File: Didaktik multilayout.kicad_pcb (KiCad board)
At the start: 2 copper layers, 212.7 x 79.4 mm, 121 parts, among them J1 Conn_01x04_MountingPin, J2 AVR-ISP-6, SW1 SW_Push_45deg, SW10 SW_Push_45deg, SW11 SW_Push_45deg, SW12 SW_Push_45deg, SW13 SW_Push_45deg, SW14 SW_Push_45deg, SW15 SW_Push_45deg, SW16 SW_Push_45deg, SW17 SW_Push_45deg, SW18 SW_Push_45deg, SW19 SW_Push_45deg, SW2 SW_Push_45deg, SW20 SW_Push_45deg, SW21 SW_Push_45deg, SW22 SW_Push_45deg, SW23 SW_Push_45deg, SW24 SW_Push_45deg, SW25 SW_Push_45deg, SW26 SW_Push_45deg, SW27 SW_Push_45deg, SW28 SW_Push_45deg, SW29 SW_Push_45deg, SW3 SW_Push_45deg, SW30 SW_Push_45deg, SW31 SW_Push_45deg, SW31a1 SW_Push_45deg, SW32 SW_Push_45deg, SW32a1 SW_Push_45deg, SW33 SW_Push_45deg, SW33a1 SW_Push_45deg, SW34 SW_Push_45deg, SW34a1 SW_Push_45deg, SW34b1 SW_Push_45deg, SW35 SW_Push_45deg, SW35a1 SW_Push_45deg, SW35b1 SW_Push_45deg, SW35c1 SW_Push_45deg, SW36 SW_Push_45deg, SW36a1 SW_Push_45deg, SW36b1 SW_Push_45deg, SW36c1 SW_Push_45deg, SW37 SW_Push_45deg, SW37a1 SW_Push_45deg, SW37b1 SW_Push_45deg, SW38 SW_Push_45deg, SW38a1 SW_Push_45deg, SW39 SW_Push_45deg, SW39a1 SW_Push_45deg, SW4 SW_Push_45deg, SW40 SW_Push_45deg, SW40a1 SW_Push_45deg, SW5 SW_Push_45deg, SW6 SW_Push_45deg, SW7 SW_Push_45deg, SW8 SW_Push_45deg, SW9 SW_Push_45deg, U1 ATmega32U4-M, Y1 Crystal_GND24_Small

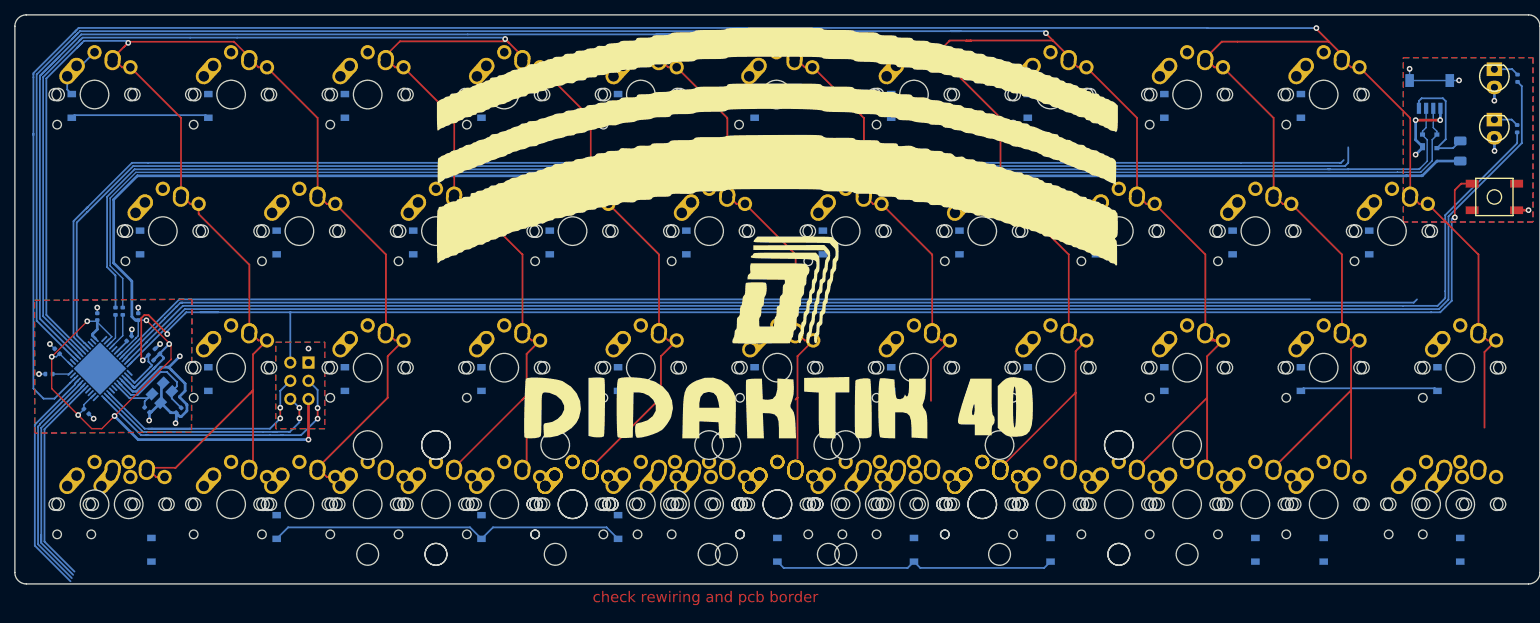
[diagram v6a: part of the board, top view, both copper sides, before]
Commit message: routing new simpler matrix on pcb
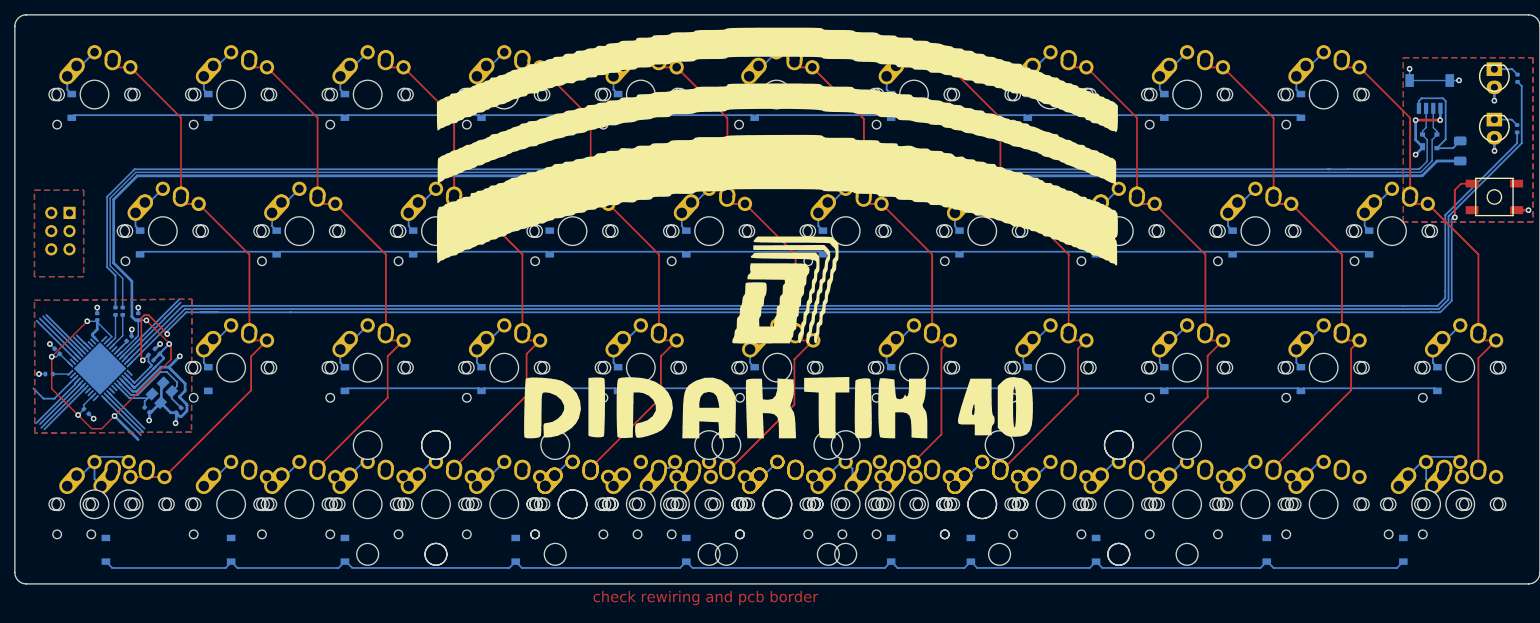
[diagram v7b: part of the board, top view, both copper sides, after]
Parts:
- moved J2 39.3 mm to (36.5, 60.3)
- moved D33 22.2 mm to (181.0, 104.8)
- moved D12 19.3 mm to (76.2, 104.8)
- moved D16 14.6 mm to (100.0, 104.8)
- moved D20 12.7 mm to (123.8, 104.8)
- moved D29 11.1 mm to (163.5, 104.8)
- moved D37 7.94 mm to (204.8, 104.8)
- moved D41 7.94 mm to (223.8, 104.8)
- moved D8 7.10 mm to (60.3, 104.8)
- moved D4 6.35 mm to (42.9, 104.8)
- moved D24 3.17 mm to (152.4, 104.8)
- turned D23 to 90 degrees
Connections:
- SW31 pad 1: unconnected-(SW31-Pad1) -> COL0
- SW32 pad 1: unconnected-(SW32-Pad1) -> COL1
- SW33 pad 1: unconnected-(SW33-Pad1) -> COL2
- SW34 pad 1: unconnected-(SW34-Pad1) -> COL3
- SW35 pad 1: unconnected-(SW35-Pad1) -> COL4
- SW36 pad 1: unconnected-(SW36-Pad1) -> COL5
- SW37 pad 1: unconnected-(SW37-Pad1) -> COL6
- SW38 pad 1: unconnected-(SW38-Pad1) -> COL7
- SW39 pad 1: unconnected-(SW39-Pad1) -> COL8
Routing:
- net COL4: track 591.5 -> 82.5 mm, vias 2 -> 0
- net COL9: track 403.6 -> 70.3 mm, vias 1 -> 0
- net COL6: track 412.3 -> 83.3 mm, vias 1 -> 0
- net COL1: track 245.4 -> 82.3 mm, vias 1 -> 0
- net COL0: track 0.00 -> 89.1 mm
- net COL3: track 0.00 -> 81.9 mm
- net COL2: track 0.00 -> 81.8 mm
- net COL5: track 0.00 -> 70.6 mm
- net ROW3: track 258.9 -> 199.0 mm
- net COL7: track 31.6 -> 82.4 mm
- net COL8: track 32.6 -> 82.7 mm
- net ROW0: track 220.3 -> 176.4 mm
- net ROW2: track 203.3 -> 165.9 mm
- net MOSI: track 39.2 -> 7.28 mm, vias 2 -> 0
- net SCK: track 38.2 -> 7.00 mm, vias 2 -> 0
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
